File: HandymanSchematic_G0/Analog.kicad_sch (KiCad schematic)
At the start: 21 parts, among them U201 TL074

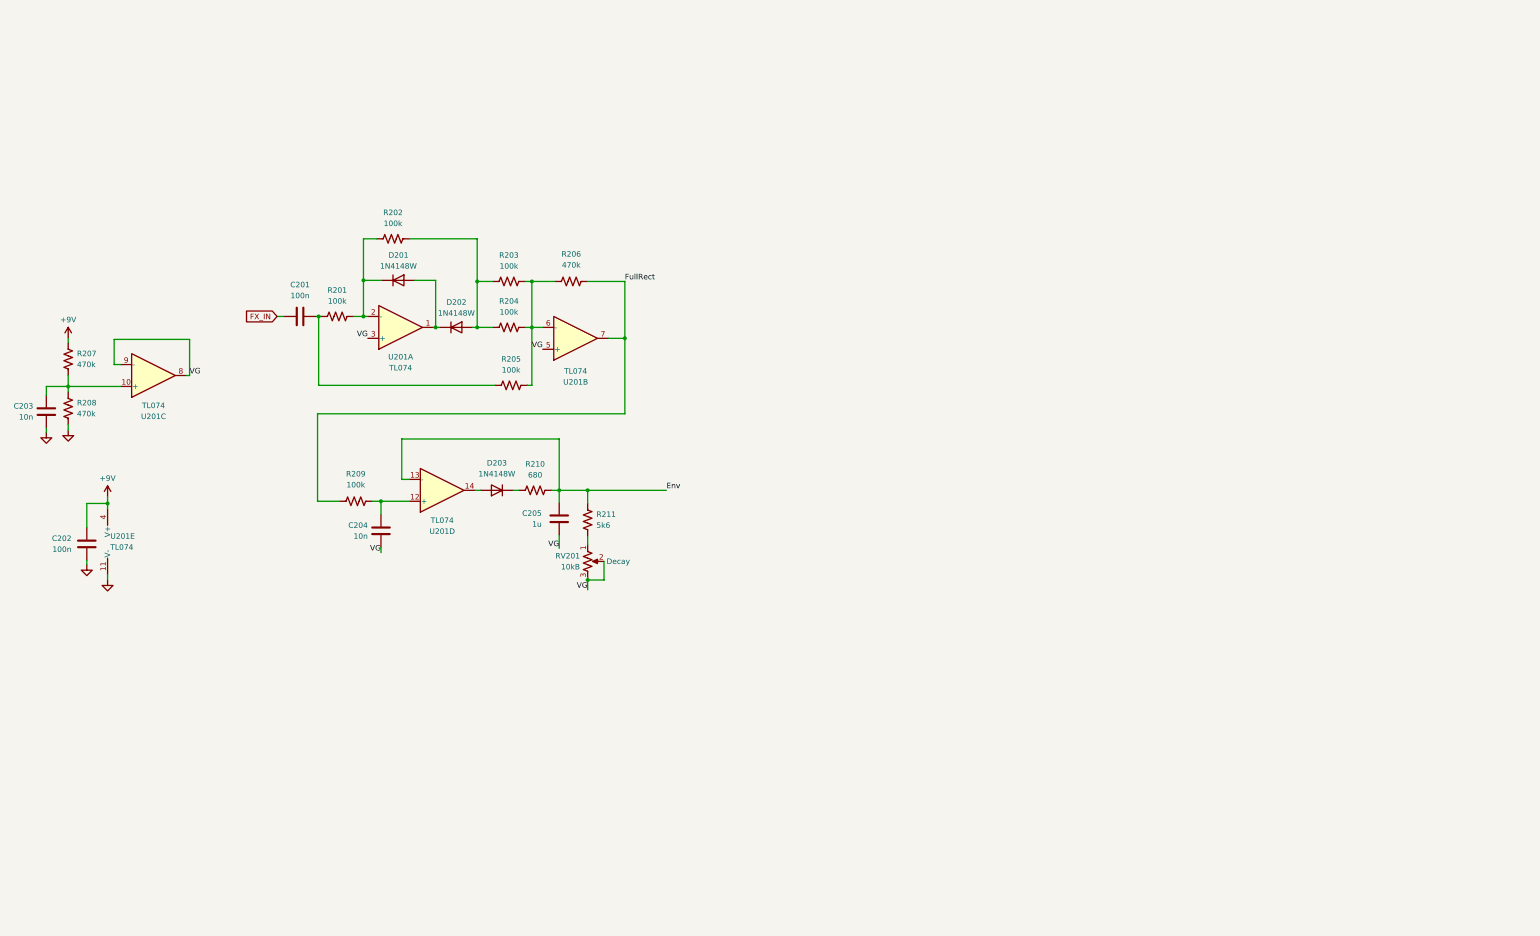
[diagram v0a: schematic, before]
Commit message: noise gate analog side schem
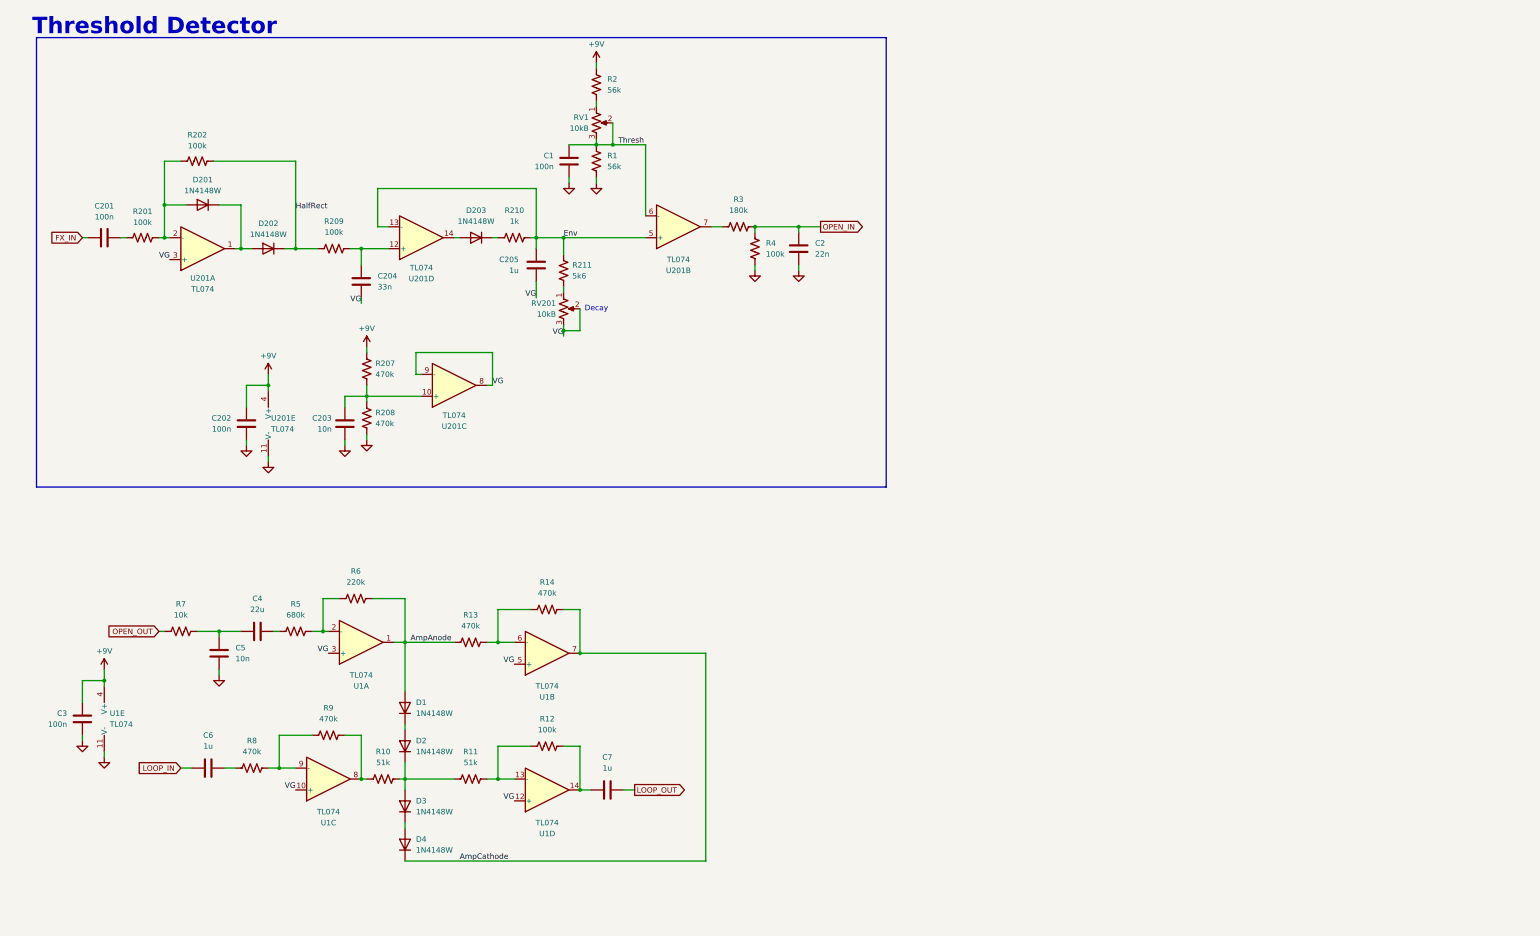
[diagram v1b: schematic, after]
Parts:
- removed R203, R204, R205: 100k, Resistor_SMD:R_0805_2012Metric, symbol Device:R_US
- removed R206: 470k, Resistor_SMD:R_0805_2012Metric, symbol Device:R_US
- added C1, C3: 100n, symbol Device:C
- added C2: 22n, symbol Device:C
- added C4: 22u, symbol Device:C
- added C5: 10n, symbol Device:C
- added C6, C7: 1u, symbol Device:C
- added D1, D2, D3, D4: 1N4148W, Diode_SMD:D_SOD-123, symbol Diode:1N4148W
- added R1, R2: 56k, symbol Device:R_US
- added R10, R11: 51k, symbol Device:R_US
- added R12, R4: 100k, symbol Device:R_US
- added R13, R14, R8, R9: 470k, symbol Device:R_US
- added R3: 180k, symbol Device:R_US
- added R5: 680k, symbol Device:R_US
- added R6: 220k, symbol Device:R_US
- added R7: 10k, symbol Device:R_US
- added RV1: 10kB, symbol Device:R_Potentiometer_US
- added U1: TL074, symbol Amplifier_Operational:TL074
- C204: value 10n -> 33n
- R210: value 680 -> 1k
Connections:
- net +9V: now also C3.1, R2.1, U1.4 (V+)
- net Env: now also U201.5 (+)
- net GND: now also C1.2, C2.2, C3.2, C5.2, R1.2, R4.2, U1.11 (V-)
- net VG: now also U1.10 (+), U1.12 (+), U1.3 (+), U1.5 (+); no longer U201.5 (+)
- net at R201.2, R202.1, U201.2 (-): now also D201.2 (A); no longer D201.1 (K)
- net at D202.2 (A): now also D201.1 (K), U201.1; no longer R202.2
- net Thresh: now reaches U201.6 (-)
- net Thresh: now also C1.1, R1.1, RV1.2, RV1.3
- net FullRect: no longer names the net of U201.7
- net FullRect: now also R3.1; no longer R209.1
- new net: D2.1 (K), D3.2 (A), R10.2, R11.1
- new net: R11.2, R12.1, U1.13 (-)
- new net: R13.2, R14.1, U1.6 (-)
- new net: C4.1, C5.1, R7.2
- new net: R5.2, R6.1, U1.2 (-)
- new net: C6.2, R8.1
- new net: R8.2, R9.1, U1.9 (-)
- new net: R2.2, RV1.1
- new net: R10.1, R9.2, U1.8
- new net: C7.1, R12.2, U1.14
- new net: D1.1 (K), D2.2 (A)
- new net: D3.1 (K), D4.2 (A)
- new net: C4.2, R5.1
- new net AmpAnode: D1.2 (A), R13.1, R6.2, U1.1
- new net AmpCathode: D4.1 (K), R14.2, U1.7
- new net HalfRect: D202.1 (K), R202.2, R209.1
- new net LOOP_IN: C6.1
- new net LOOP_OUT: C7.2
- new net OPEN_IN: C2.1, R3.2, R4.1
- new net OPEN_OUT: R7.1
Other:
- note added: "Threshold Detector"
- moved on the sheet: C201, C202, C203, C204, C205, D201, D202, D203, R201, R202, R207, R208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

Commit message: tuner input circuitry
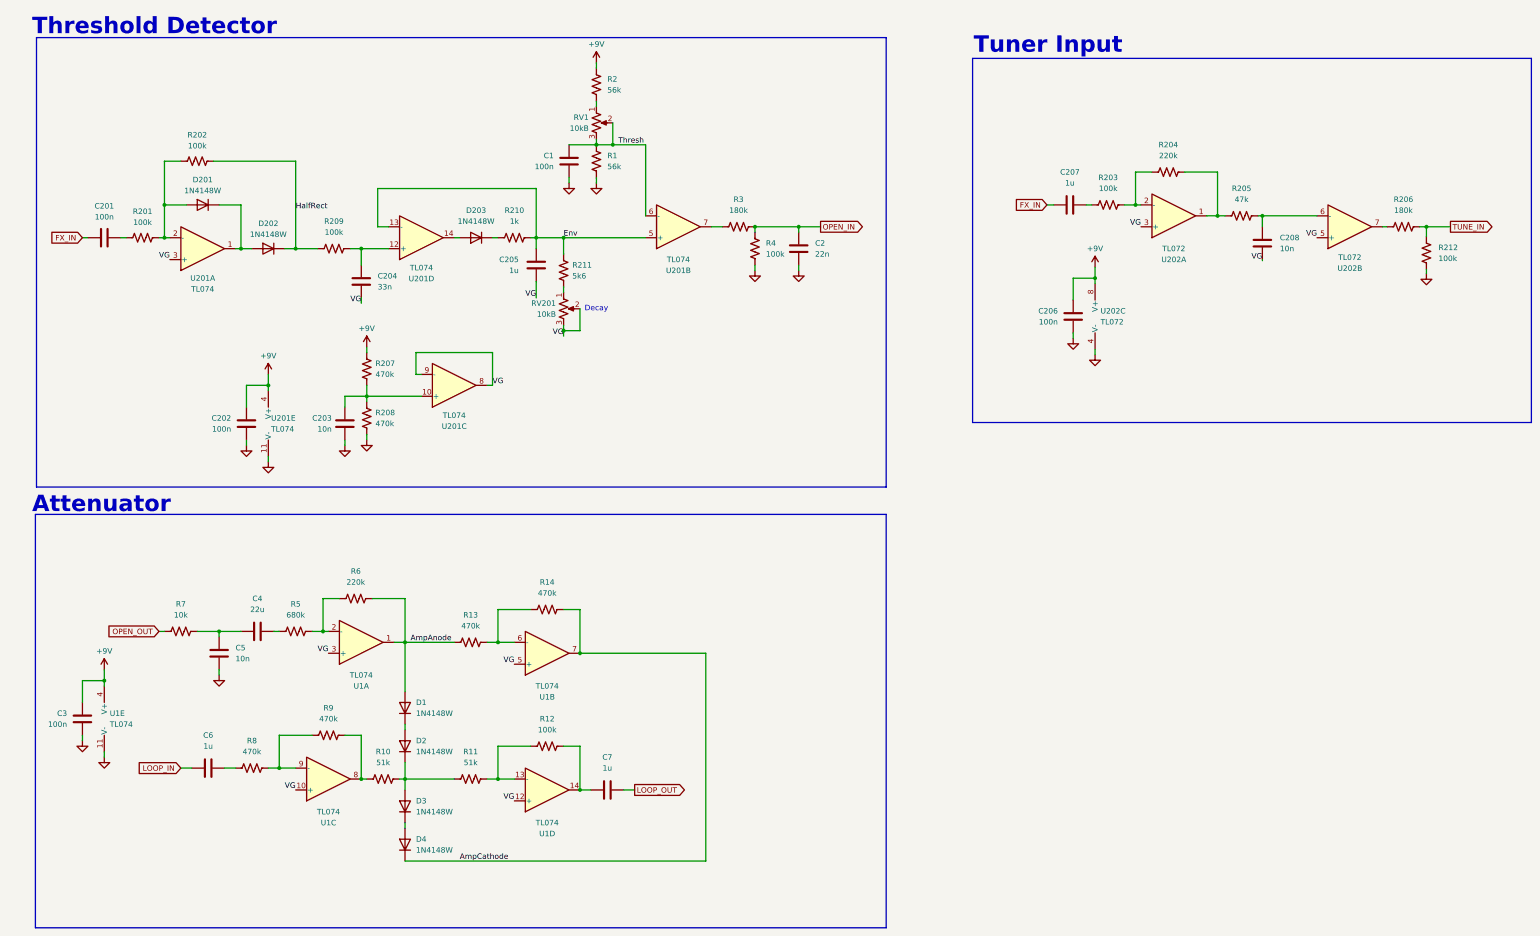
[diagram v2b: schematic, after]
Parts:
- added C206: 100n, symbol Device:C
- added C207: 1u, symbol Device:C
- added C208: 10n, symbol Device:C
- added R203, R212: 100k, symbol Device:R_US
- added R204: 220k, symbol Device:R_US
- added R205: 47k, symbol Device:R_US
- added R206: 180k, symbol Device:R_US
- added U202: TL072, symbol Amplifier_Operational:TL072
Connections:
- net +9V: now also C206.1, U202.8 (V+)
- net FX_IN: now also C207.1
- net GND: now also C206.2, R212.1, U202.4 (V-)
- net VG: now also C208.1, U202.3 (+), U202.5 (+)
- new net: R206.1, U202.7
- new net: R203.2, R204.1, U202.2 (-)
- new net: R204.2, R205.1, U202.1
- new net: C208.2, R205.2, U202.6 (-)
- new net: C207.2, R203.1
- new net TUNE_IN: R206.2, R212.2
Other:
- note added: "Attenuator"
- note added: "Tuner Input"

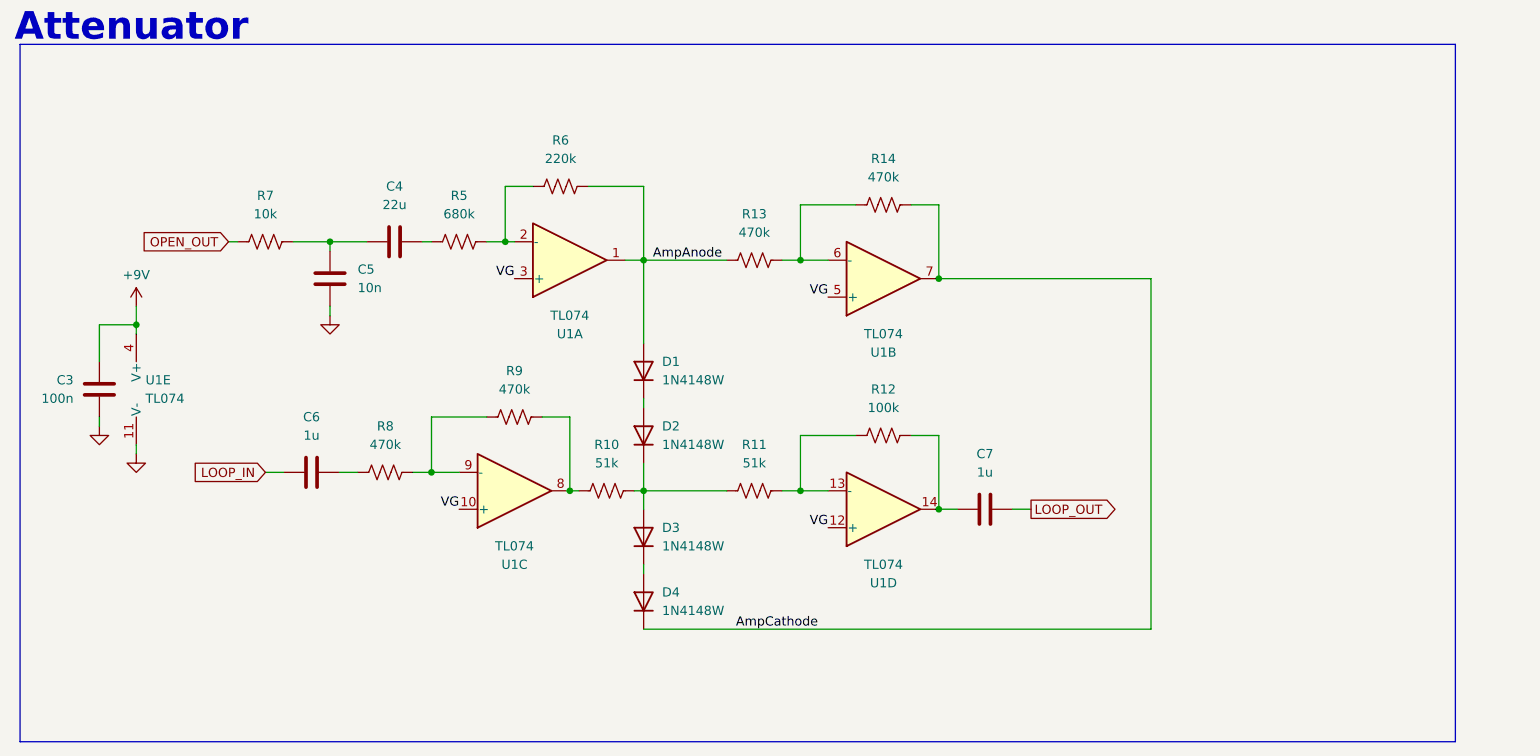
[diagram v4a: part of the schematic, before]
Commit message: attenuator input change
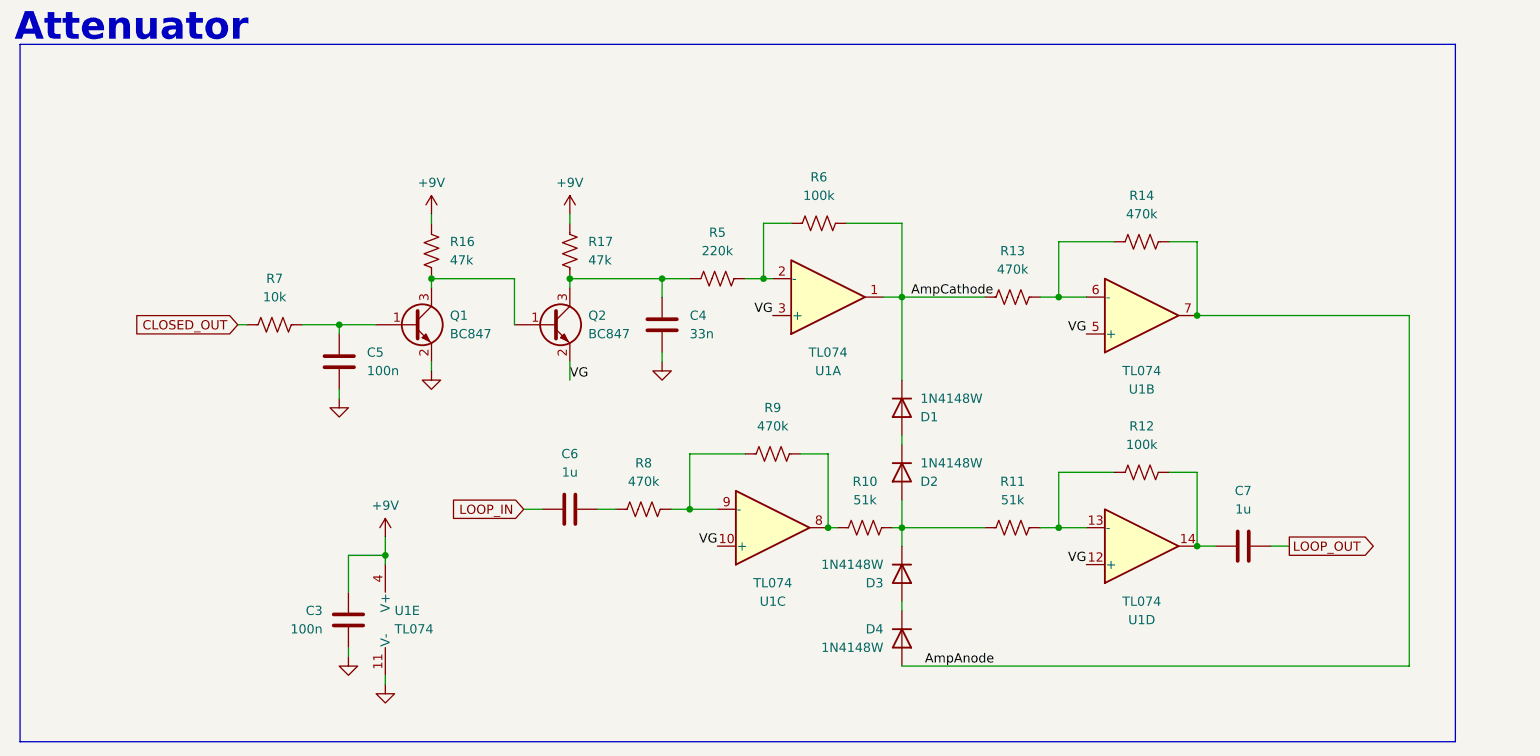
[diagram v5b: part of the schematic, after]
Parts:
- added Q1, Q2: BC847, Package_TO_SOT_SMD:SOT-23, symbol Transistor_BJT:BC847
- added R16, R17: 47k, symbol Device:R_US
- C4: value 22u -> 33n
- C5: value 10n -> 100n
- R5: value 680k -> 220k
- R6: value 220k -> 100k
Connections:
- net +9V: now also R16.1, R17.1
- net AmpAnode: now also D4.2 (A), R14.2, U1.7; no longer D1.2 (A), R13.1, R6.2, U1.1
- net AmpCathode: now also D1.1 (K), R13.1, R6.2, U1.1; no longer D4.1 (K), R14.2, U1.7
- net GND: now also C4.2, Q1.2 (E)
- net VG: now also Q2.2 (E)
- net at R10.2, R11.1: now also D2.2 (A), D3.1 (K); no longer D2.1 (K), D3.2 (A)
- net at C5.1, R7.2: now also Q1.1 (B); no longer C4.1
- net at R5.1: now also C4.1, Q2.3 (C), R17.2; no longer C4.2
- net OPEN_OUT renamed CLOSED_OUT
- new net: Q1.3 (C), Q2.1 (B), R16.2
- new net: D1.2 (A), D2.1 (K)
- new net: D3.2 (A), D4.1 (K)
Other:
- moved on the sheet: C3, C5, C6, C7, D1, D2, D3, D4, R10, R11, R12, R13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
